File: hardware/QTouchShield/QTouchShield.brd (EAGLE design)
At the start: 100 x 80 mm, 114 parts, among them IC1 AT32UC3C0512C, U1 ARDUINO-MEGALITE

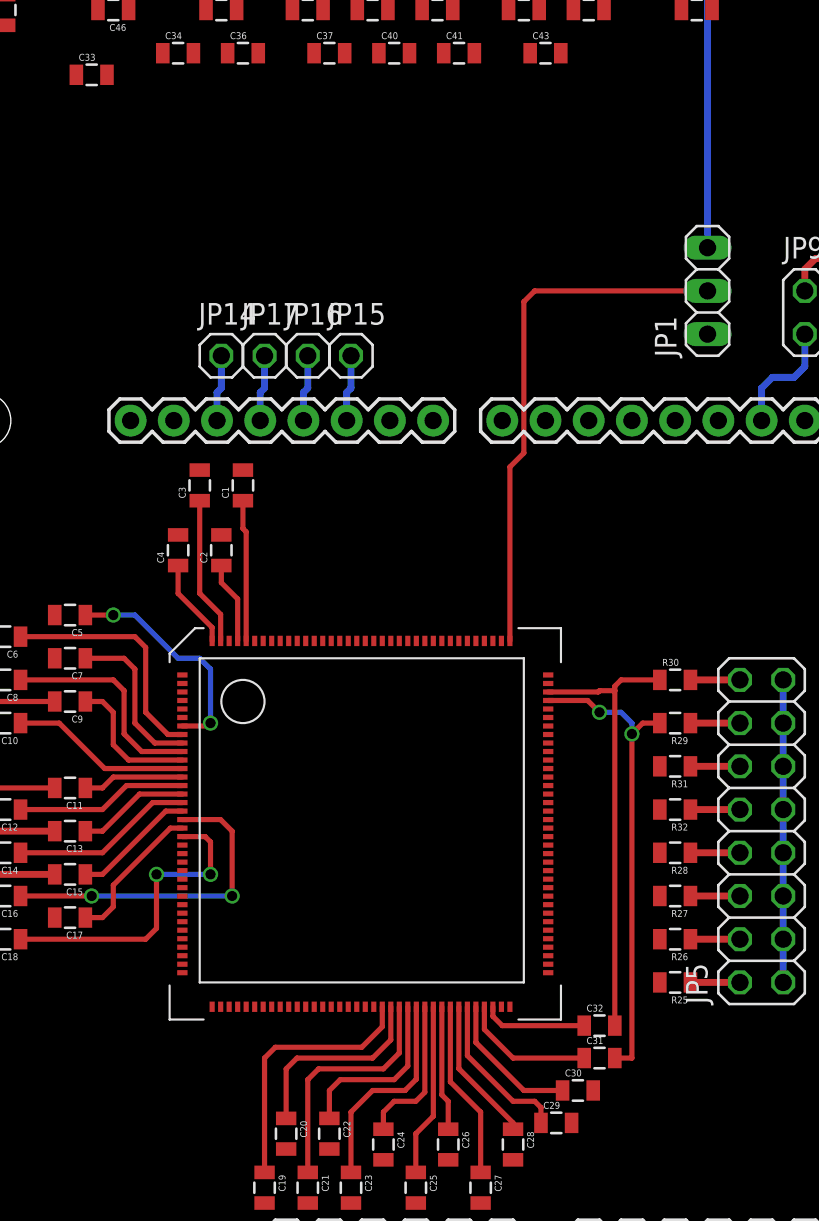
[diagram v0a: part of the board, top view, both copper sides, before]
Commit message: Changed LQFP-144 footprint.
Ripped up LQFP-144 package footprint and replaced by footprint from an
offical EagleCAD library.
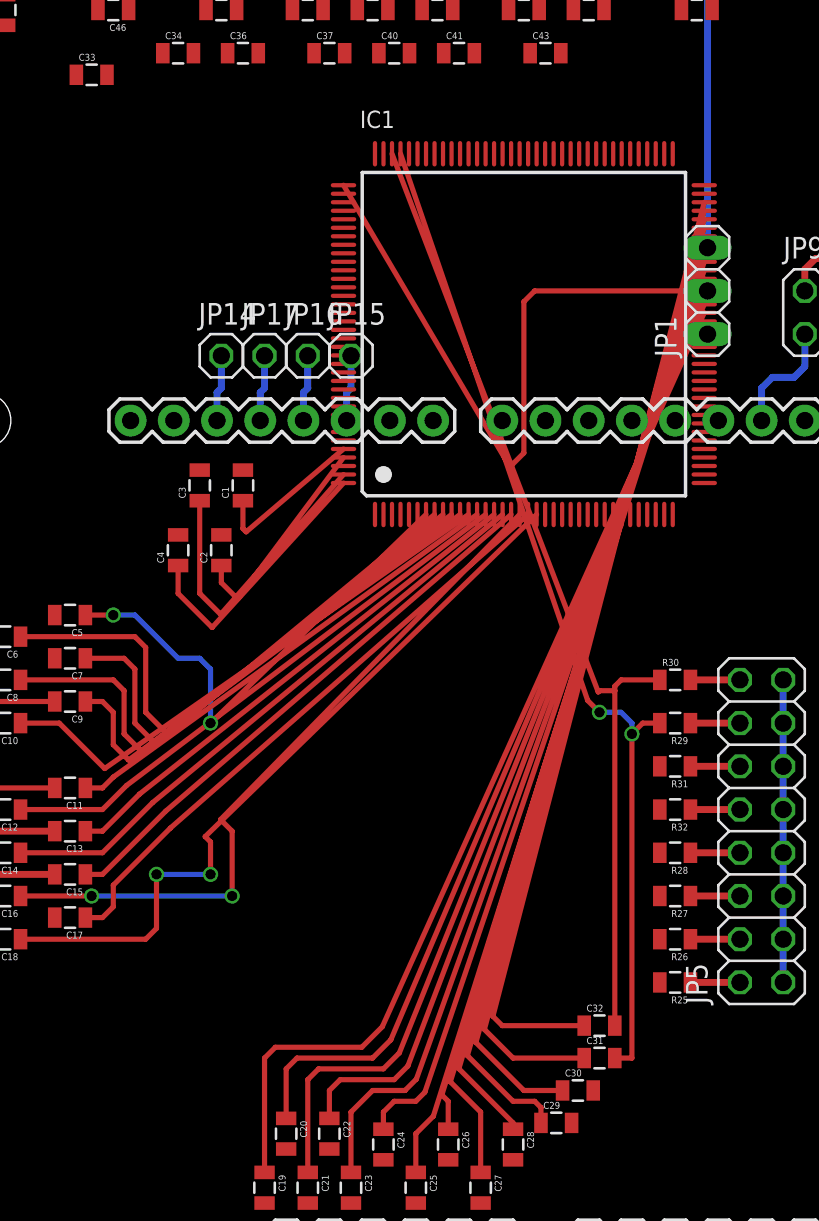
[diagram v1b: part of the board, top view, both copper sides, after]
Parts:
- IC1: value AT32UC3C0512C -> AT32UC3C0512CJEDEC-MS-026
- moved IC1 27.0 mm to (47.0, 57.1)
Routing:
- net SNS31: track 6.15 -> 55.0 mm
- net SNS30: track 7.89 -> 56.4 mm
- net SNS29: track 8.36 -> 56.5 mm
- net SNS28: track 9.36 -> 57.1 mm
- net SNS27: track 8.51 -> 55.9 mm
- net SNS26: track 10.5 -> 57.5 mm
- net SNS25: track 7.35 -> 54.0 mm
- net SNS24: track 10.2 -> 56.4 mm
- net SNS23: track 8.95 -> 54.9 mm
- net SNS22: track 12.4 -> 58.2 mm
- net SNS21: track 10.3 -> 55.8 mm
- net SNS20: track 14.2 -> 59.4 mm
- net SNS19: track 11.7 -> 56.8 mm
- net SNS18: track 15.6 -> 60.4 mm
- net SNSK30: track 28.1 -> 59.7 mm
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
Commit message: Rotated AT32UC3C packge to correct position.
Package was at wrong angle related to the related components. Fixed.
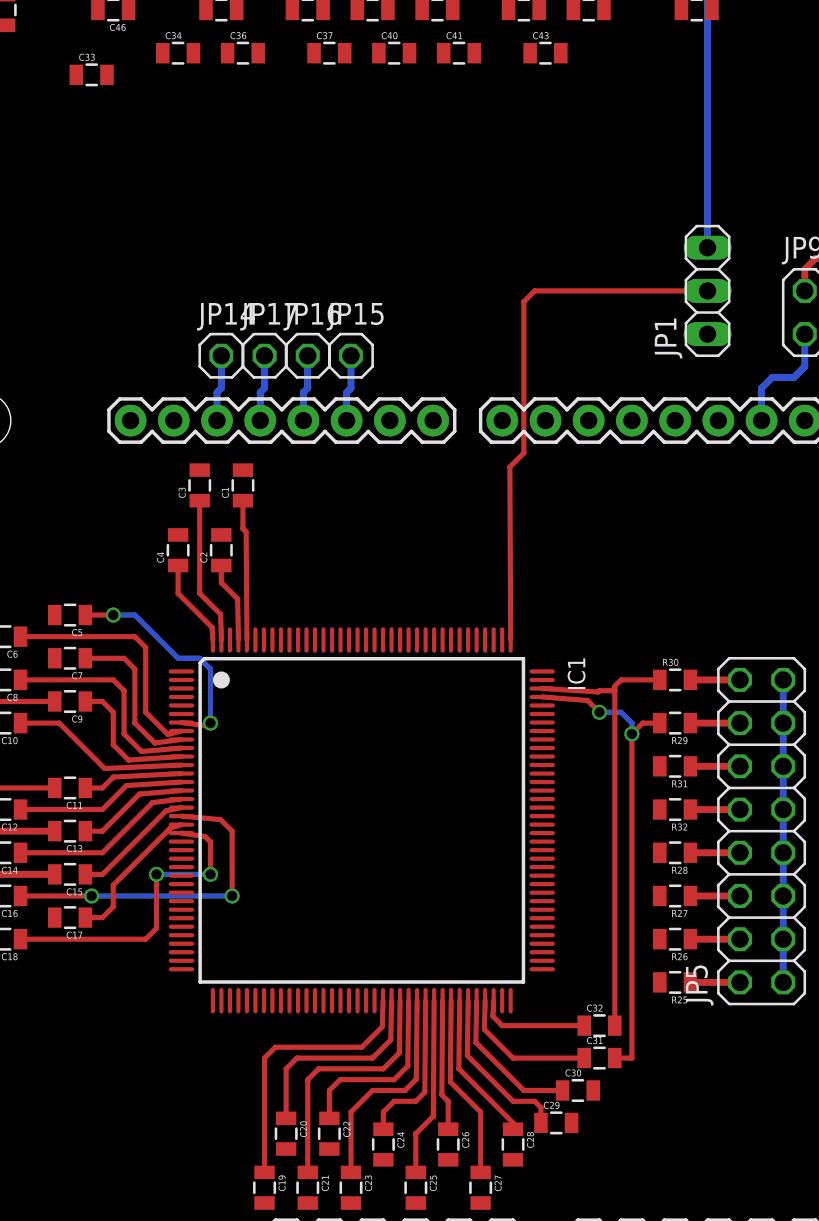
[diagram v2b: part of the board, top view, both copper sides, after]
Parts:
- moved IC1 30.1 mm to (37.5, 28.6), turned to 270 degrees
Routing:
- net SNS31: track 55.0 -> 6.51 mm
- net SNS30: track 56.4 -> 8.25 mm
- net SNS29: track 56.5 -> 8.72 mm
- net SNS28: track 57.1 -> 9.72 mm
- net SNS27: track 55.9 -> 8.87 mm
- net SNS26: track 57.5 -> 10.8 mm
- net SNS25: track 54.0 -> 7.71 mm
- net SNS24: track 56.4 -> 10.5 mm
- net SNS23: track 54.9 -> 9.30 mm
- net SNS22: track 58.2 -> 12.8 mm
- net SNS21: track 55.8 -> 10.7 mm
- net SNS20: track 59.4 -> 14.6 mm
- net SNS19: track 56.8 -> 12.1 mm
- net SNS18: track 60.4 -> 15.9 mm
- net SNSK30: track 59.7 -> 28.4 mm
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
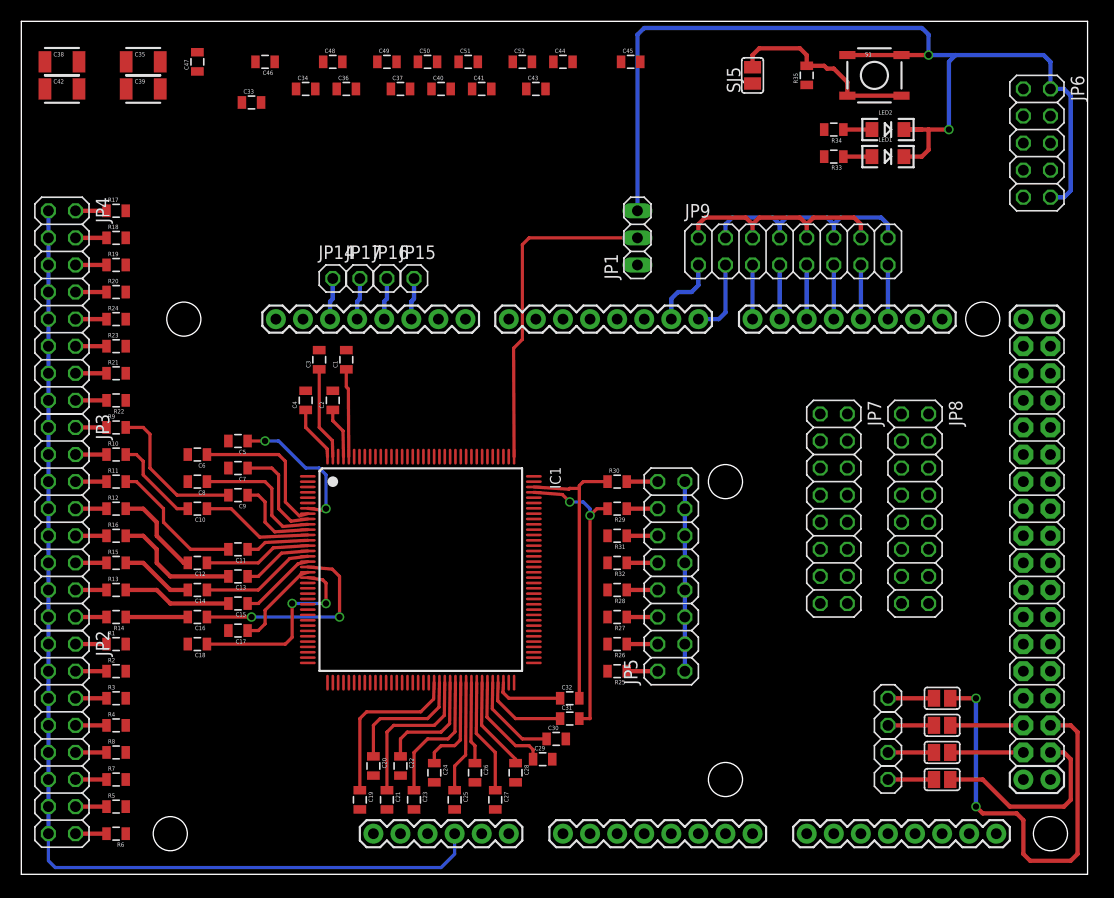
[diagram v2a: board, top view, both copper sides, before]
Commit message: Move hardware to 4-layer board.
32-Touch channels in a reasonable board space was not working out. Moved
to 4-layer board.
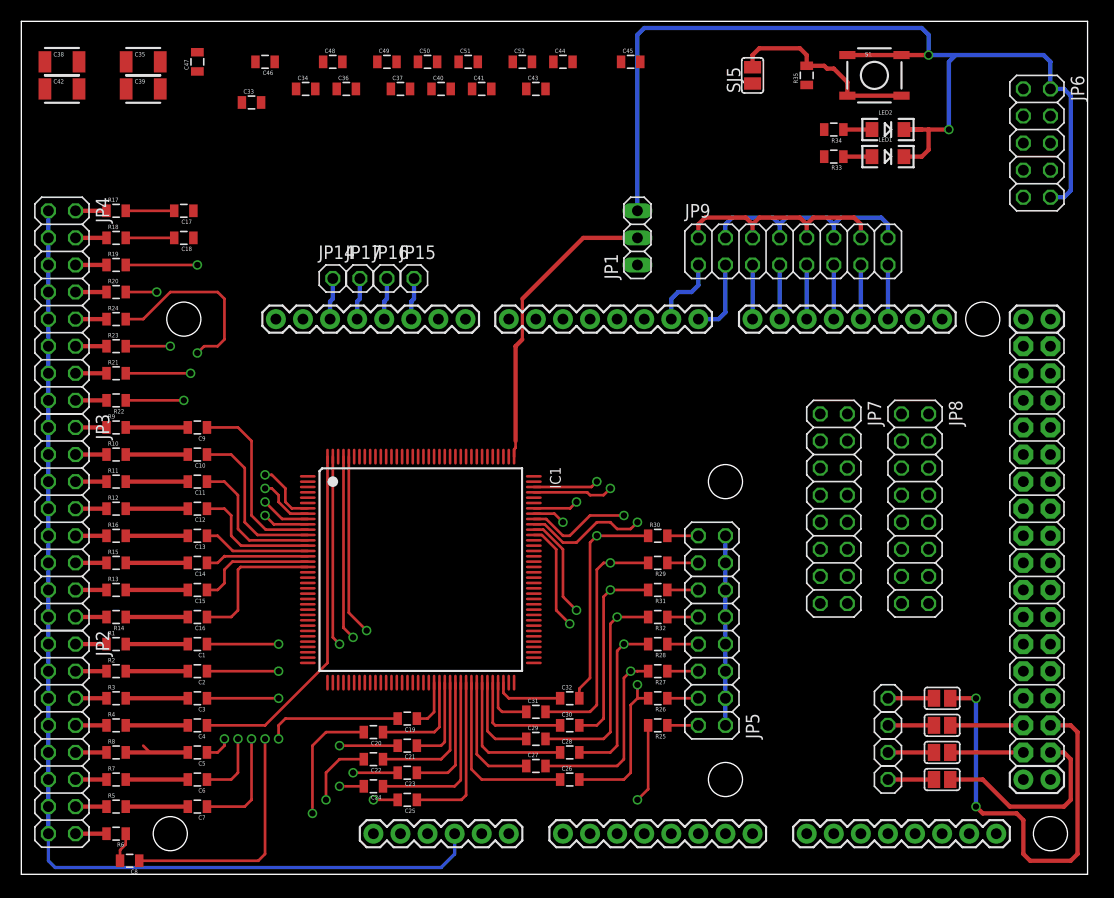
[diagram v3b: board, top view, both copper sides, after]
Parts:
- moved C17 39.7 mm to (15.2, 62.2)
- moved C18 38.1 mm to (15.2, 59.7)
- moved C8 36.1 mm to (10.2, 1.27)
- moved C3 33.7 mm to (16.5, 16.5), turned to 180 degrees
- moved C4 32.1 mm to (16.5, 14.0), turned to 180 degrees
- moved C7 32.0 mm to (16.5, 6.35)
- moved C6 30.5 mm to (16.5, 8.89)
- moved C1 30.1 mm to (16.5, 21.6), turned to 180 degrees
- moved C5 29.5 mm to (16.5, 11.4)
- moved C2 28.4 mm to (16.5, 19.1), turned to 180 degrees
- moved C26 8.91 mm to (51.4, 8.89), turned to 0 degrees
- moved C19 8.82 mm to (36.2, 14.6), turned to 180 degrees
- moved C11 7.41 mm to (16.5, 36.8)
- moved C9 7.41 mm to (16.5, 41.9)
- moved JP5 6.35 mm to (64.8, 22.9)
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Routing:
- net SNSK19: track 0.00 -> 76.6 mm, vias 0 -> 2
- net SNSK20: track 0.00 -> 75.0 mm, vias 0 -> 2
- net SNSK18: track 0.00 -> 72.5 mm, vias 0 -> 2
- net SNSK21: track 0.00 -> 67.2 mm, vias 0 -> 2
- net SNSK22: track 0.00 -> 63.7 mm, vias 0 -> 2
- net SNSK24: track 0.00 -> 61.1 mm, vias 0 -> 3
- net SNSK23: track 0.00 -> 59.1 mm, vias 0 -> 2
- net SNSK26: track 0.00 -> 43.8 mm, vias 0 -> 2
- net SNSK27: track 0.00 -> 38.4 mm, vias 0 -> 2
- net SNSK25: track 0.00 -> 36.3 mm, vias 0 -> 2
- net SNSK28: track 0.00 -> 36.2 mm, vias 0 -> 2
- net SNS7: track 12.7 -> 48.2 mm, vias 0 -> 2
- net SNSK29: track 0.00 -> 33.0 mm, vias 0 -> 2
- net SNS1: track 4.77 -> 34.0 mm, vias 0 -> 2
- net SNS6: track 9.58 -> 37.9 mm, vias 0 -> 2
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
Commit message: Further routing added on SNS and SNSK lines.
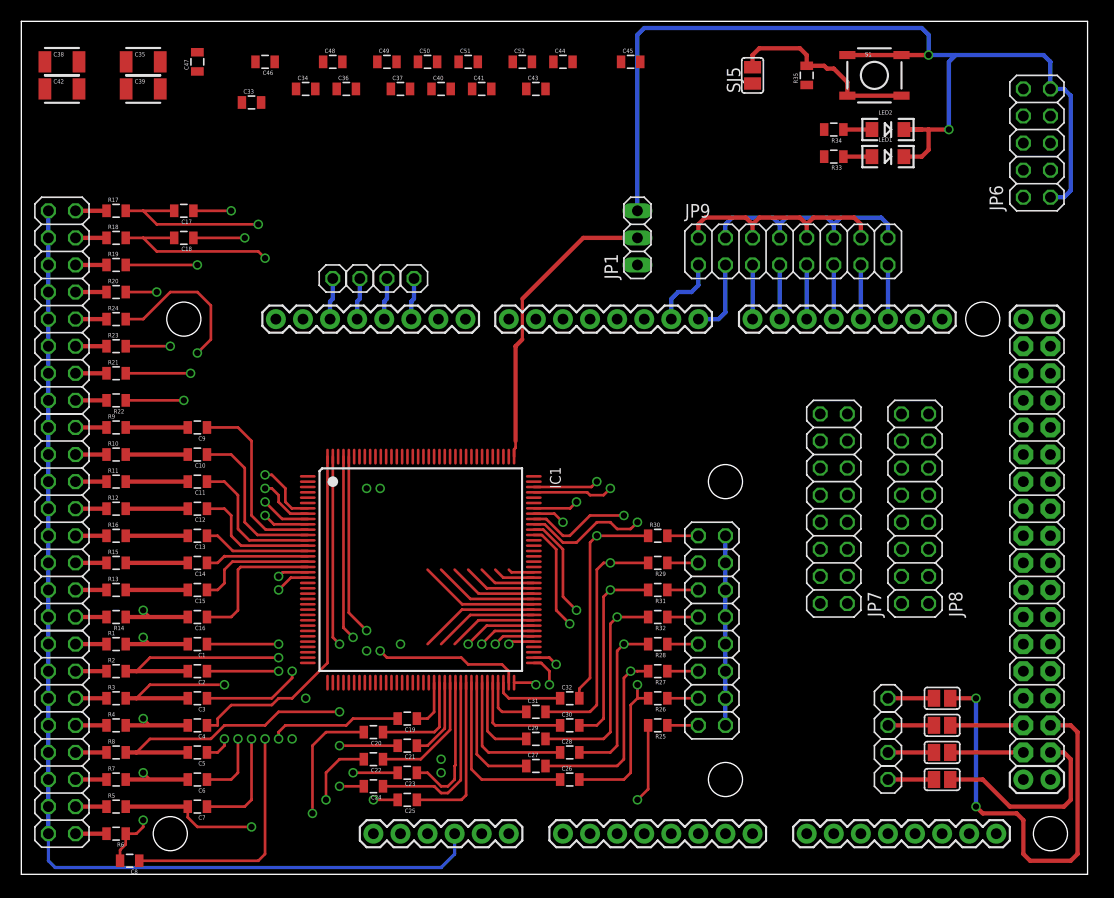
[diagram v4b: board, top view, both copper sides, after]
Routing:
- net SNSK5: track 5.82 -> 60.0 mm, vias 0 -> 4
- net SNSK4: track 10.3 -> 62.9 mm, vias 0 -> 3
- net SNSK2: track 5.82 -> 57.4 mm, vias 0 -> 3
- net SNSK3: track 5.82 -> 56.0 mm, vias 0 -> 3
- net SNSK7: track 2.76 -> 50.6 mm, vias 0 -> 2
- net SNSK1: track 5.82 -> 52.6 mm, vias 0 -> 3
- net SNSK0: track 5.82 -> 51.8 mm, vias 0 -> 2
- net SNSK16: track 4.55 -> 49.8 mm, vias 0 -> 2
- net SNS17: track 0.00 -> 43.9 mm, vias 0 -> 2
- net SNS16: track 0.00 -> 42.6 mm, vias 0 -> 2
- net SNSK17: track 4.55 -> 46.3 mm, vias 0 -> 2
- net SNSK6: track 5.82 -> 47.3 mm, vias 0 -> 2
- net SNSK15: track 5.82 -> 42.5 mm, vias 0 -> 1
- net SNSK11: track 5.82 -> 17.1 mm
- net SNSK10: track 5.82 -> 17.1 mm
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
